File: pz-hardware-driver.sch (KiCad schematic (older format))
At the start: 0 parts

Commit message: More changes to the basic layout.
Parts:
- added D1: Auger Triac, symbol Device:Q_TRIAC_A1A2G
- added D2: Fan Triac, symbol Device:Q_TRIAC_A1A2G
- added D3: Rod Triac, symbol Device:Q_TRIAC_A1A2G
- added D4: Fan Triac, symbol Device:LED
- added D5: Rod LED, symbol Device:LED
- added D6: Auger LED, symbol Device:LED
- added J1: RTD 1-2, symbol Connector:Screw_Terminal_01x06
- added J2: RTD 3-4, symbol Connector:Screw_Terminal_01x06
- added J3: Auger Conn, symbol Connector:Conn_01x02_Male
- added J4: Fan Conn, symbol Connector:Conn_01x02_Male
- added J5: Rod Conn, symbol Connector:Conn_01x02_Male
- added J6: RTD 5-6, symbol Connector:Screw_Terminal_01x06
- added J7: Logic Header, symbol Connector_Generic:Conn_02x15_Counter_Clockwise
- added J8: Display, symbol Connector_Generic:Conn_01x06
- added J?: Enhanced, symbol Connector:Screw_Terminal_01x06
- added P1: Wall Plug, symbol Connector:Conn_WallPlug_Earth
- added R1: AUG, symbol Device:R_Small
- added R2: FAN, symbol Device:R_Small
- added R3: ROD, symbol Device:R_Small
- added T1: Transformer, Transformer_THT:Transformer_Microphone_Lundahl_LL1538, symbol Device:Transformer_1P_SS
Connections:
- net labels added: +3.3V, +5V, AC_N, AC_P, AUG, Earth, FAN, GND, ROD
- wire segments 0 -> 11

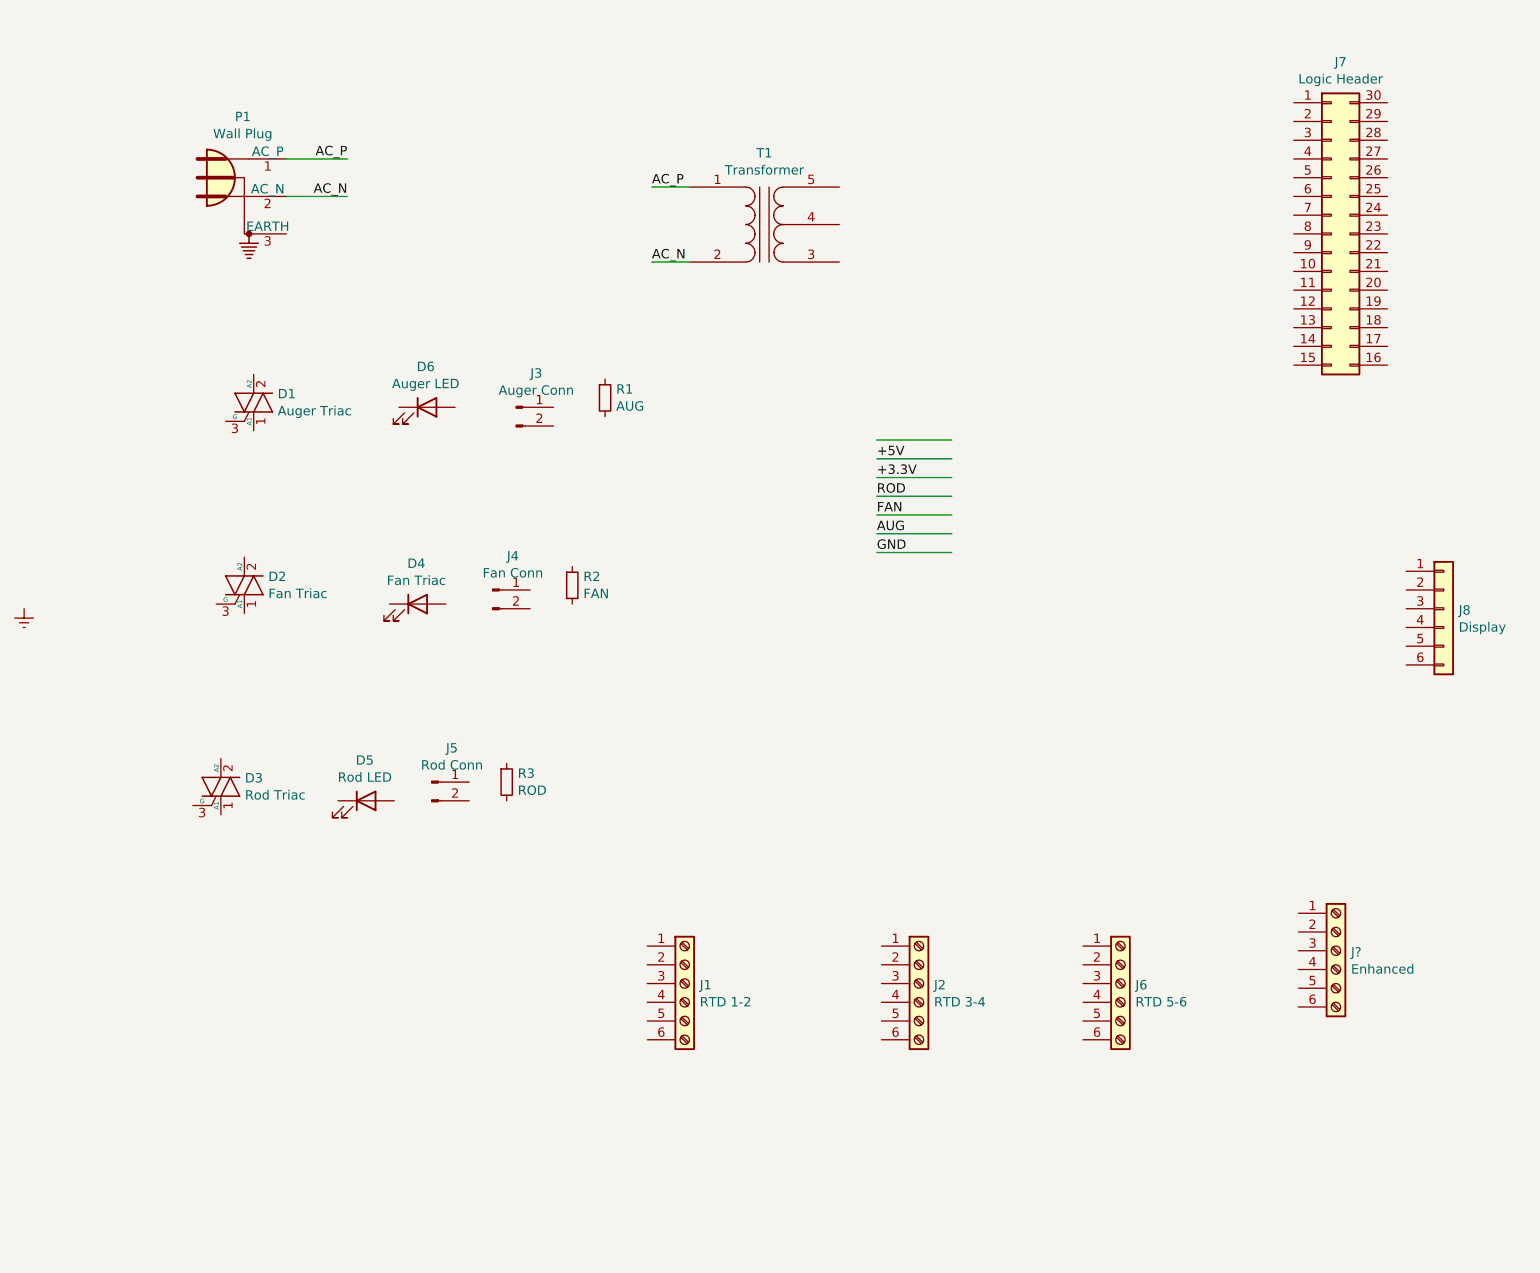
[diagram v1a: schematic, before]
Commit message: Added the transformer, a few LEDs, the optocoupler. All these need more work.
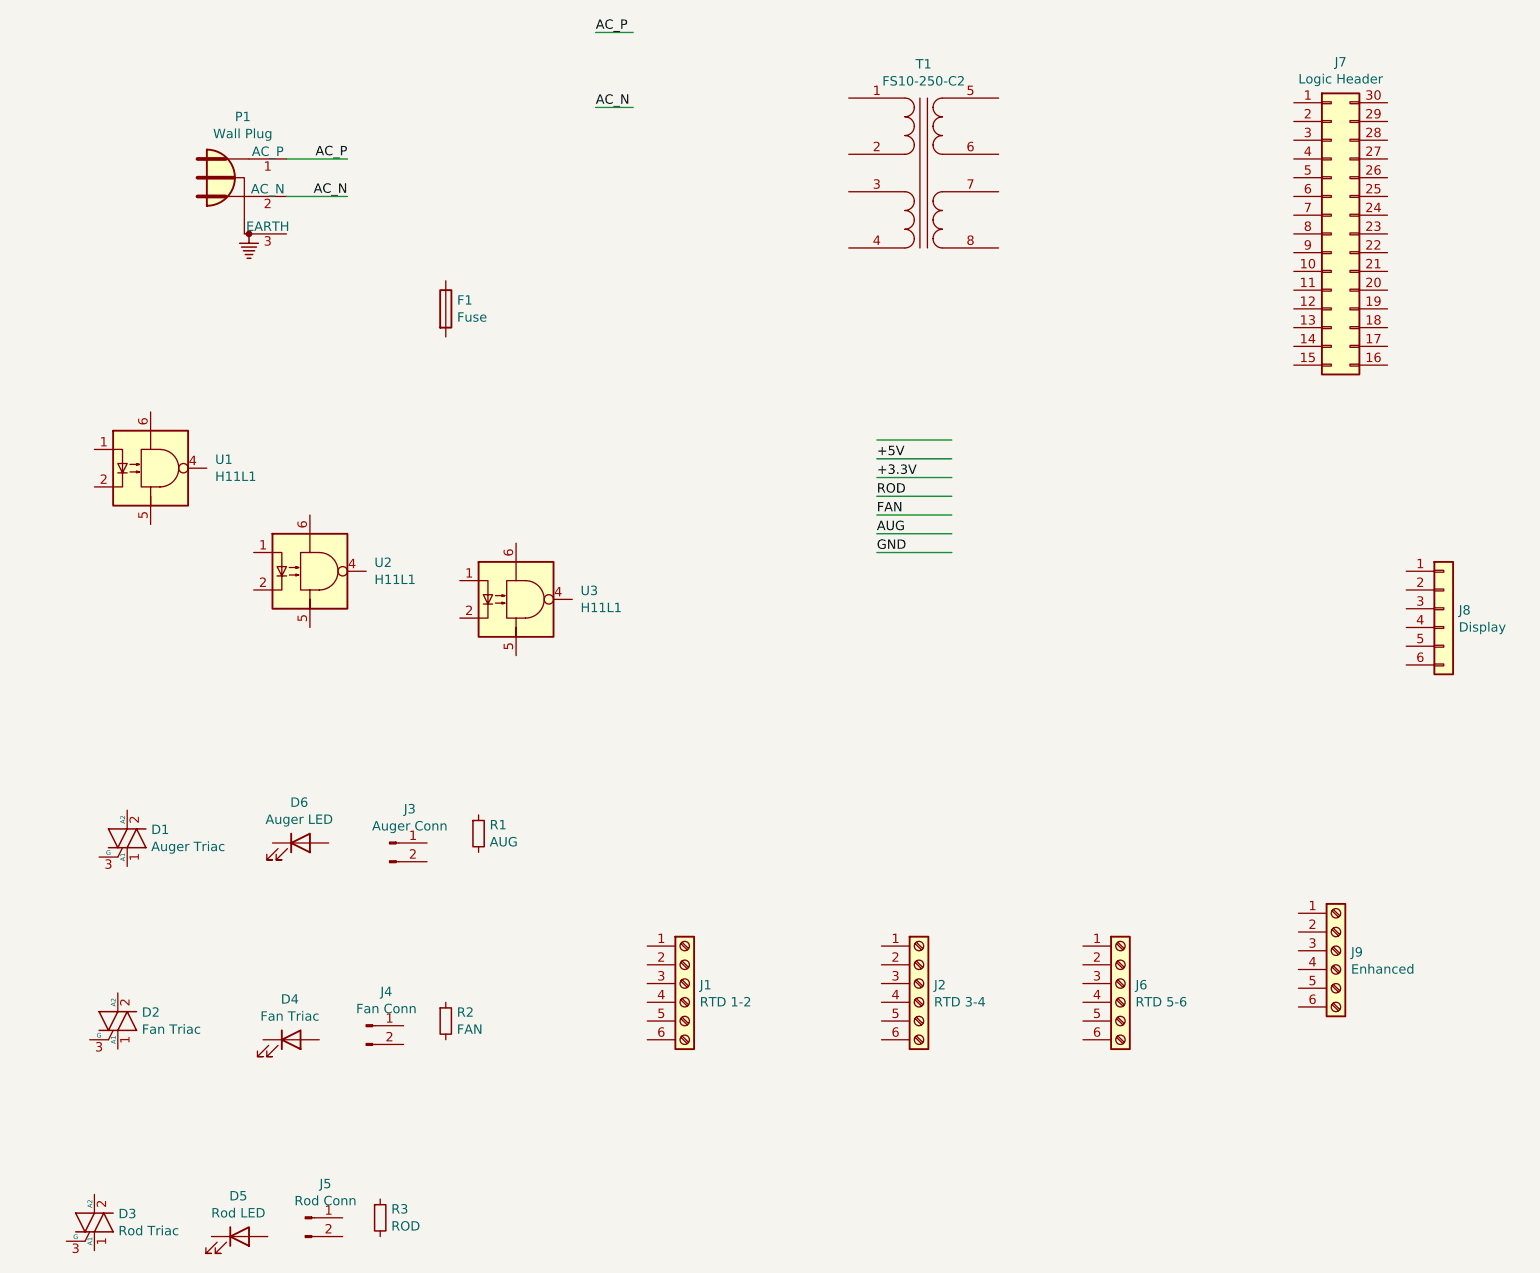
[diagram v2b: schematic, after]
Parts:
- removed T1: Transformer, Transformer_THT:Transformer_Microphone_Lundahl_LL1538, symbol Device:Transformer_1P_SS
- added F1: Fuse, symbol Device:Fuse
- added T1: FS10-250-C2, pz-hardware-driver:FS10-250-C2, symbol pz-hardware-driver:FS10-250-C2
- added U1, U2, U3: H11L1, symbol Isolator:H11L1
- gave numbers to parts that had none: 1
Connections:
- net labels removed: Earth
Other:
- moved on the sheet: D1, D2, D3, D4, D5, D6, J3, J4, J5, R1, R2, R3
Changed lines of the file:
@@
 Comment4 ""
 $EndDescr
-$Comp
-L power:Earth #PWR0102
-U 1 1 5DF4923F
-P 800 4075
-F 0 "#PWR0102" H 800 3825 50  0001 C CNN
-F 1 "Earth" H 800 3925 50  0001 C CNN
-F 2 "" H 800 4075 50  0001 C CNN
-F 3 "~" H 800 4075 50  0001 C CNN
-	1    800  4075
-	1    0    0    -1
-$EndComp
-$Comp
-L Device:Transformer_1P_SS T1
-U 1 1 5E06AD5C
-P 4750 2025
-F 0 "T1" H 4750 2406 50  0000 C CNN
-F 1 "Transformer" H 4750 2315 50  0000 C CNN
-F 2 "Transformer_THT:Transformer_Microphone_Lundahl_LL1538" H 4750 2025 50  0001 C CNN
-F 3 "~" H 4750 2025 50  0001 C CNN
-	1    4750 2025
-	1    0    0    -1
-$EndComp
-Wire Wire Line
-	4350 1825 4150 1825
-Wire Wire Line
-	4350 2225 4150 2225
-Text Label 4150 2225 0    50   ~ 0
+Wire Wire Line
+	4050 1000 3850 1000
+Wire Wire Line
+	4050 1400 3850 1400
+Text Label 3850 1400 0    50   ~ 0
 AC_N
 $Comp
@@
 L Connector:Conn_01x02_Male J3
 U 1 1 5E077F05
-P 3425 3000
-F 0 "J3" H 3533 3181 50  0000 C CNN
-F 1 "Auger Conn" H 3533 3090 50  0000 C CNN
-F 2 "" H 3425 3000 50  0001 C CNN
-F 3 "~" H 3425 3000 50  0001 C CNN
-	1    3425 3000
+P 2750 5325
+F 0 "J3" H 2858 5506 50  0000 C CNN
+F 1 "Auger Conn" H 2858 5415 50  0000 C CNN
+F 2 "" H 2750 5325 50  0001 C CNN
+F 3 "~" H 2750 5325 50  0001 C CNN
+	1    2750 5325
 	1    0    0    -1
 $EndComp
@@
 L Connector:Conn_01x02_Male J4
 U 1 1 5E07858E
-P 3300 3975
-F 0 "J4" H 3408 4156 50  0000 C CNN
-F 1 "Fan Conn" H 3408 4065 50  0000 C CNN
-F 2 "" H 3300 3975 50  0001 C CNN
-F 3 "~" H 3300 3975 50  0001 C CNN
-	1    3300 3975
+P 2625 6300
+F 0 "J4" H 2733 6481 50  0000 C CNN
+F 1 "Fan Conn" H 2733 6390 50  0000 C CNN
+F 2 "" H 2625 6300 50  0001 C CNN
+F 3 "~" H 2625 6300 50  0001 C CNN
+	1    2625 6300
 	1    0    0    -1
 $EndComp
@@
 L Connector:Conn_01x02_Male J5
 U 1 1 5E078BB5
-P 2975 5000
-F 0 "J5" H 3083 5181 50  0000 C CNN
-F 1 "Rod Conn" H 3083 5090 50  0000 C CNN
-F 2 "" H 2975 5000 50  0001 C CNN
-F 3 "~" H 2975 5000 50  0001 C CNN
-	1    2975 5000
+P 2300 7325
+F 0 "J5" H 2408 7506 50  0000 C CNN
+F 1 "Rod Conn" H 2408 7415 50  0000 C CNN
+F 2 "" H 2300 7325 50  0001 C CNN
+F 3 "~" H 2300 7325 50  0001 C CNN
+	1    2300 7325
 	1    0    0    -1
 $EndComp
@@
 L Device:LED D6
 U 1 1 5E0799FF
-P 2950 3000
-F 0 "D6" H 2943 3216 50  0000 C CNN
-F 1 "Auger LED" H 2943 3125 50  0000 C CNN
-F 2 "" H 2950 3000 50  0001 C CNN
-F 3 "~" H 2950 3000 50  0001 C CNN
-	1    2950 3000
+P 2275 5325
+F 0 "D6" H 2268 5541 50  0000 C CNN
+F 1 "Auger LED" H 2268 5450 50  0000 C CNN
+F 2 "" H 2275 5325 50  0001 C CNN
+F 3 "~" H 2275 5325 50  0001 C CNN
+	1    2275 5325
 	1    0    0    -1
 $EndComp
@@
 L Device:LED D4
 U 1 1 5E079E9E
-P 2900 4050
-F 0 "D4" H 2893 4266 50  0000 C CNN
-F 1 "Fan Triac" H 2893 4175 50  0000 C CNN
-F 2 "" H 2900 4050 50  0001 C CNN
-F 3 "~" H 2900 4050 50  0001 C CNN
-	1    2900 4050
+P 2225 6375
+F 0 "D4" H 2218 6591 50  0000 C CNN
+F 1 "Fan Triac" H 2218 6500 50  0000 C CNN
+F 2 "" H 2225 6375 50  0001 C CNN
+F 3 "~" H 2225 6375 50  0001 C CNN
+	1    2225 6375
 	1    0    0    -1
 $EndComp
@@
 L Device:LED D5
 U 1 1 5E07A261
-P 2625 5100
-F 0 "D5" H 2618 5316 50  0000 C CNN
-F 1 "Rod LED" H 2618 5225 50  0000 C CNN
-F 2 "" H 2625 5100 50  0001 C CNN
-F 3 "~" H 2625 5100 50  0001 C CNN
-	1    2625 5100
+P 1950 7425
+F 0 "D5" H 1943 7641 50  0000 C CNN
+F 1 "Rod LED" H 1943 7550 50  0000 C CNN
+F 2 "" H 1950 7425 50  0001 C CNN
+F 3 "~" H 1950 7425 50  0001 C CNN
+	1    1950 7425
 	1    0    0    -1
 $EndComp
@@
 L Device:Q_TRIAC_A1A2G D1
 U 1 1 5E07ACBD
-P 2025 2975
-F 0 "D1" H 2153 3021 50  0000 L CNN
-F 1 "Auger Triac" H 2153 2930 50  0000 L CNN
-F 2 "" V 2100 3000 50  0001 C CNN
-F 3 "~" V 2025 2975 50  0001 C CNN
-	1    2025 2975
+P 1350 5300
+F 0 "D1" H 1478 5346 50  0000 L CNN
+F 1 "Auger Triac" H 1478 5255 50  0000 L CNN
+F 2 "" V 1425 5325 50  0001 C CNN
+F 3 "~" V 1350 5300 50  0001 C CNN
+	1    1350 5300
 	1    0    0    -1
 $EndComp
@@
 L Device:Q_TRIAC_A1A2G D2
 U 1 1 5E07B684
-P 1975 3950
-F 0 "D2" H 2103 3996 50  0000 L CNN
-F 1 "Fan Triac" H 2103 3905 50  0000 L CNN
-F 2 "" V 2050 3975 50  0001 C CNN
-F 3 "~" V 1975 3950 50  0001 C CNN
-	1    1975 3950
+P 1300 6275
+F 0 "D2" H 1428 6321 50  0000 L CNN
+F 1 "Fan Triac" H 1428 6230 50  0000 L CNN
+F 2 "" V 1375 6300 50  0001 C CNN
+F 3 "~" V 1300 6275 50  0001 C CNN
+	1    1300 6275
 	1    0    0    -1
 $EndComp
@@
 L Device:Q_TRIAC_A1A2G D3
 U 1 1 5E07BB62
-P 1850 5025
-F 0 "D3" H 1978 5071 50  0000 L CNN
-F 1 "Rod Triac" H 1978 4980 50  0000 L CNN
-F 2 "" V 1925 5050 50  0001 C CNN
-F 3 "~" V 1850 5025 50  0001 C CNN
-	1    1850 5025
+P 1175 7350
+F 0 "D3" H 1303 7396 50  0000 L CNN
+F 1 "Rod Triac" H 1303 7305 50  0000 L CNN
+F 2 "" V 1250 7375 50  0001 C CNN
+F 3 "~" V 1175 7350 50  0001 C CNN
+	1    1175 7350
 	1    0    0    -1
 $EndComp
@@
 Text Label 5350 3675 0    50   ~ 0
 AUG
-Text Label 4150 1825 0    50   ~ 0
+Text Label 3850 1000 0    50   ~ 0
 AC_P
 $Comp
 L Device:R_Small R1
 U 1 1 5E08588F
-P 3900 2950
-F 0 "R1" H 3959 2996 50  0000 L CNN
-F 1 "AUG" H 3959 2905 50  0000 L CNN
-F 2 "" H 3900 2950 50  0001 C CNN
-F 3 "~" H 3900 2950 50  0001 C CNN
-	1    3900 2950
+P 3225 5275
+F 0 "R1" H 3284 5321 50  0000 L CNN
+F 1 "AUG" H 3284 5230 50  0000 L CNN
+F 2 "" H 3225 5275 50  0001 C CNN
+F 3 "~" H 3225 5275 50  0001 C CNN
+	1    3225 5275
 	1    0    0    -1
 $EndComp
@@
 L Device:R_Small R2
 U 1 1 5E085C81
-P 3725 3950
-F 0 "R2" H 3784 3996 50  0000 L CNN
-F 1 "FAN" H 3784 3905 50  0000 L CNN
-F 2 "" H 3725 3950 50  0001 C CNN
-F 3 "~" H 3725 3950 50  0001 C CNN
-	1    3725 3950
+P 3050 6275
+F 0 "R2" H 3109 6321 50  0000 L CNN
+F 1 "FAN" H 3109 6230 50  0000 L CNN
+F 2 "" H 3050 6275 50  0001 C CNN
+F 3 "~" H 3050 6275 50  0001 C CNN
+	1    3050 6275
 	1    0    0    -1
 $EndComp
@@
 L Device:R_Small R3
 U 1 1 5E085F7B
-P 3375 5000
-F 0 "R3" H 3434 5046 50  0000 L CNN
-F 1 "ROD" H 3434 4955 50  0000 L CNN
-F 2 "" H 3375 5000 50  0001 C CNN
-F 3 "~" H 3375 5000 50  0001 C CNN
-	1    3375 5000
+P 2700 7325
+F 0 "R3" H 2759 7371 50  0000 L CNN
+F 1 "ROD" H 2759 7280 50  0000 L CNN
+F 2 "" H 2700 7325 50  0001 C CNN
+F 3 "~" H 2700 7325 50  0001 C CNN
+	1    2700 7325
 	1    0    0    -1
 $EndComp
@@
 $EndComp
 $Comp
-L Connector:Screw_Terminal_01x06 J?
+L Connector:Screw_Terminal_01x06 J9
 U 1 1 5E260B0E
 P 7800 5900
-F 0 "J?" H 7880 5892 50  0000 L CNN
+F 0 "J9" H 7880 5892 50  0000 L CNN
 F 1 "Enhanced" H 7880 5801 50  0000 L CNN
 F 2 "" H 7800 5900 50  0001 C CNN
@@
 	1    0    0    -1
 $EndComp
+$Comp
+L Device:Fuse F1
+U 1 1 5E3F5B1D
+P 3050 2475
+F 0 "F1" H 3110 2521 50  0000 L CNN
+F 1 "Fuse" H 3110 2430 50  0000 L CNN
+F 2 "" V 2980 2475 50  0001 C CNN
+F 3 "~" H 3050 2475 50  0001 C CNN
+	1    3050 2475
+	1    0    0    -1
+$EndComp
+$Comp
+L Isolator:H11L1 U2
+U 1 1 5E3F6C0C
+P 2325 3875
+F 0 "U2" H 2669 3921 50  0000 L CNN
+F 1 "H11L1" H 2669 3830 50  0000 L CNN
+F 2 "" H 2235 3875 50  0001 C CNN
+F 3 "https://www.fairchildsemi.com/datasheets/H1/H11L1M.pdf" H 2235 3875 50  0001 C CNN
+	1    2325 3875
+	1    0    0    -1
+$EndComp
+$Comp
+L Isolator:H11L1 U3
+U 1 1 5E3F7DEF
+P 3425 4025
+F 0 "U3" H 3769 4071 50  0000 L CNN
+F 1 "H11L1" H 3769 3980 50  0000 L CNN
+F 2 "" H 3335 4025 50  0001 C CNN
+F 3 "https://www.fairchildsemi.com/datasheets/H1/H11L1M.pdf" H 3335 4025 50  0001 C CNN
+	1    3425 4025
+	1    0    0    -1
+$EndComp
+$Comp
+L Isolator:H11L1 U1
+U 1 1 5E3F873C
+P 1475 3325
+F 0 "U1" H 1819 3371 50  0000 L CNN
+F 1 "H11L1" H 1819 3280 50  0000 L CNN
+F 2 "" H 1385 3325 50  0001 C CNN
+F 3 "https://www.fairchildsemi.com/datasheets/H1/H11L1M.pdf" H 1385 3325 50  0001 C CNN
+	1    1475 3325
+	1    0    0    -1
+$EndComp
+$Comp
+L pz-hardware-driver:FS10-250-C2 T1
+U 1 1 5E3FCC78
+P 5600 1750
+F 0 "T1" H 5600 2331 50  0000 C CNN
+F 1 "FS10-250-C2" H 5600 2240 50  0000 C CNN
+F 2 "pz-hardware-driver:FS10-250-C2" H 5600 1750 50  0001 C CNN
+F 3 "~" H 5600 1750 50  0001 C CNN
+	1    5600 1750
+	1    0    0    -1
+$EndComp
